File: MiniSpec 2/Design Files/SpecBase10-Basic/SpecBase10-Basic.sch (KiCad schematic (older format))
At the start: 3 parts, among them J1 M20-8770642R, J2 M20-8770642R, J3 Conn_01x04_Male

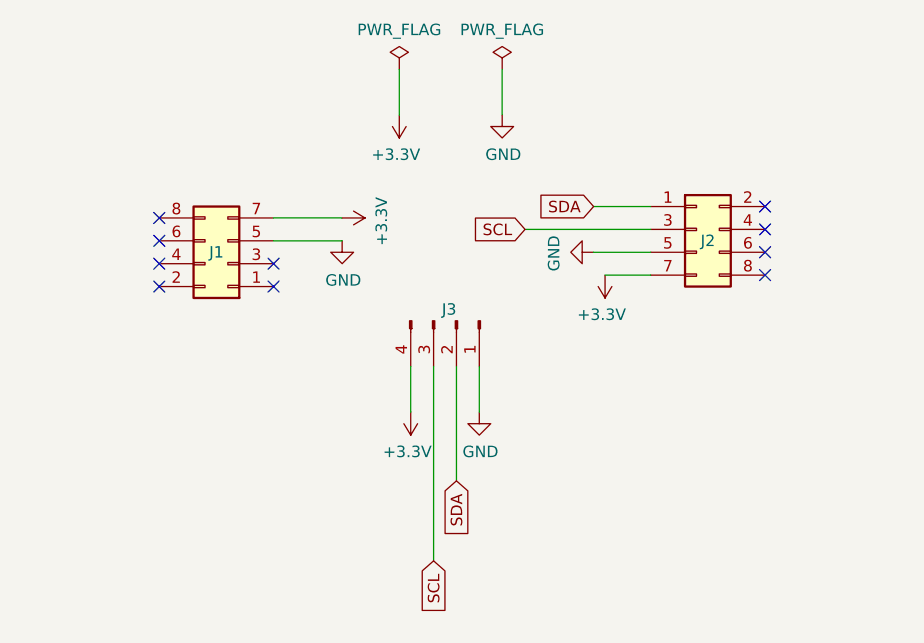
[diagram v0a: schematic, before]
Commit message: Finished I2C Bus Board, added raw data of spec readings
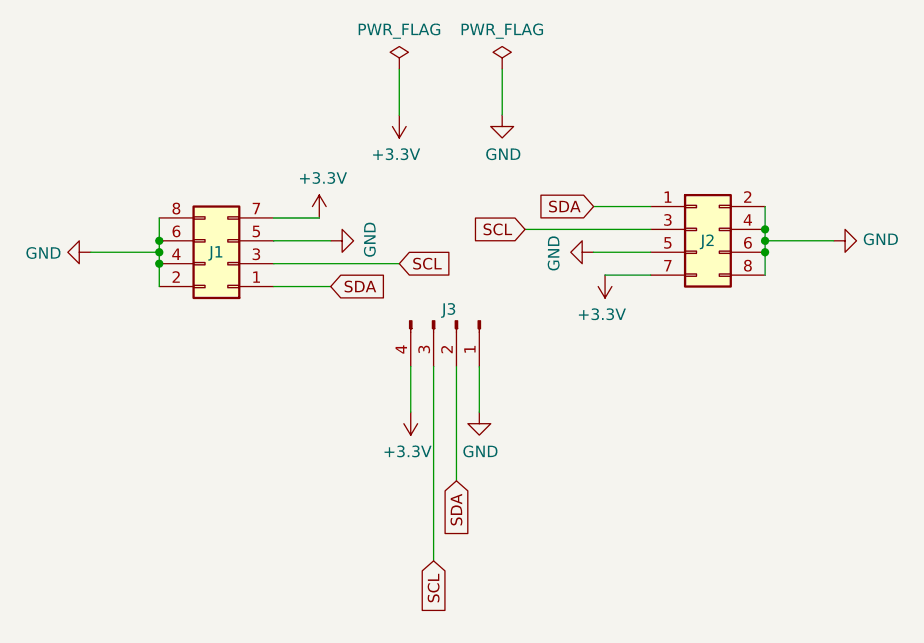
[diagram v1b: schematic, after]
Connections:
- net GND: now also J1.2 (Pin_2), J1.4 (Pin_4), J1.6 (Pin_6), J1.8 (Pin_8), J2.2 (Pin_2), J2.4 (Pin_4), J2.6 (Pin_6), J2.8 (Pin_8)
- net SCL: now also J1.3 (Pin_3)
- net SDA: now also J1.1 (Pin_1)
- no-connect marks 10 -> 0
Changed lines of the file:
@@
 Text GLabel 5450 5550 3    50   Input ~ 0
 SCL
-$Comp
-L power:+3.3V #PWR0105
-U 1 1 5F463F88
-P 5050 4050
-F 0 "#PWR0105" H 5050 3900 50  0001 C CNN
-F 1 "+3.3V" H 5065 4223 50  0000 C CNN
-F 2 "" H 5050 4050 50  0001 C CNN
-F 3 "" H 5050 4050 50  0001 C CNN
-	1    5050 4050
-	0    1    1    0
-$EndComp
-Wire Wire Line
-	5050 4150 4750 4150
-$Comp
-L power:GND #PWR0107
-U 1 1 5F464CC9
-P 5050 4150
-F 0 "#PWR0107" H 5050 3900 50  0001 C CNN
-F 1 "GND" H 5055 3977 50  0000 C CNN
-F 2 "" H 5050 4150 50  0001 C CNN
-F 3 "" H 5050 4150 50  0001 C CNN
-	1    5050 4150
-	1    0    0    -1
-$EndComp
-Wire Wire Line
-	4750 4050 5050 4050
 Wire Wire Line
 	5450 5550 5450 4700
-NoConn ~ 6900 4000
-NoConn ~ 6900 4100
-NoConn ~ 6900 4200
-NoConn ~ 6900 4300
-NoConn ~ 4250 4050
-NoConn ~ 4250 4150
-NoConn ~ 4250 4250
-NoConn ~ 4250 4350
-NoConn ~ 4750 4250
-NoConn ~ 4750 4350
 Wire Wire Line
 	6150 4000 6400 4000
@@
 Wire Wire Line
 	5550 5200 5550 4700
+$Comp
+L power:GND #PWR?
+U 1 1 5F61031B
+P 3950 4200
+F 0 "#PWR?" H 3950 3950 50  0001 C CNN
+F 1 "GND" V 3955 4072 50  0000 R CNN
+F 2 "" H 3950 4200 50  0001 C CNN
+F 3 "" H 3950 4200 50  0001 C CNN
+	1    3950 4200
+	0    1    1    0
+$EndComp
+Wire Wire Line
+	4250 4050 4250 4150
+Connection ~ 4250 4150
+Wire Wire Line
+	4250 4150 4250 4200
+Connection ~ 4250 4250
+Wire Wire Line
+	4250 4250 4250 4350
+Wire Wire Line
+	4250 4200 3950 4200
+Connection ~ 4250 4200
+Wire Wire Line
+	4250 4200 4250 4250
+Wire Wire Line
+	6900 4000 6900 4100
+Connection ~ 6900 4100
+Wire Wire Line
+	6900 4100 6900 4150
+Connection ~ 6900 4200
+Wire Wire Line
+	6900 4200 6900 4300
+$Comp
+L power:GND #PWR?
+U 1 1 5F611F13
+P 7200 4150
+F 0 "#PWR?" H 7200 3900 50  0001 C CNN
+F 1 "GND" V 7205 4022 50  0000 R CNN
+F 2 "" H 7200 4150 50  0001 C CNN
+F 3 "" H 7200 4150 50  0001 C CNN
+	1    7200 4150
+	0    -1   -1   0
+$EndComp
+Wire Wire Line
+	6900 4150 7200 4150
+Connection ~ 6900 4150
+Wire Wire Line
+	6900 4150 6900 4200
+Wire Wire Line
+	5000 4350 4750 4350
+Wire Wire Line
+	5300 4250 4750 4250
+Text GLabel 5000 4350 2    50   Input ~ 0
+SDA
+Text GLabel 5300 4250 2    50   Input ~ 0
+SCL
+Wire Wire Line
+	4750 4050 4950 4050
+Wire Wire Line
+	4750 4150 5000 4150
+$Comp
+L power:+3.3V #PWR?
+U 1 1 5F6131D0
+P 4950 4050
+F 0 "#PWR?" H 4950 3900 50  0001 C CNN
+F 1 "+3.3V" H 4965 4223 50  0000 C CNN
+F 2 "" H 4950 4050 50  0001 C CNN
+F 3 "" H 4950 4050 50  0001 C CNN
+	1    4950 4050
+	1    0    0    -1
+$EndComp
+$Comp
+L power:GND #PWR?
+U 1 1 5F6131D6
+P 5000 4150
+F 0 "#PWR?" H 5000 3900 50  0001 C CNN
+F 1 "GND" H 5005 3977 50  0000 C CNN
+F 2 "" H 5000 4150 50  0001 C CNN
+F 3 "" H 5000 4150 50  0001 C CNN
+	1    5000 4150
+	0    -1   -1   0
+$EndComp
 $EndSCHEMATC
